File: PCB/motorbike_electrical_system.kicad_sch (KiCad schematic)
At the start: 11 parts, among them U1 L7805, U2 L7805, U3 L7805, U4 ATmega16L-8P

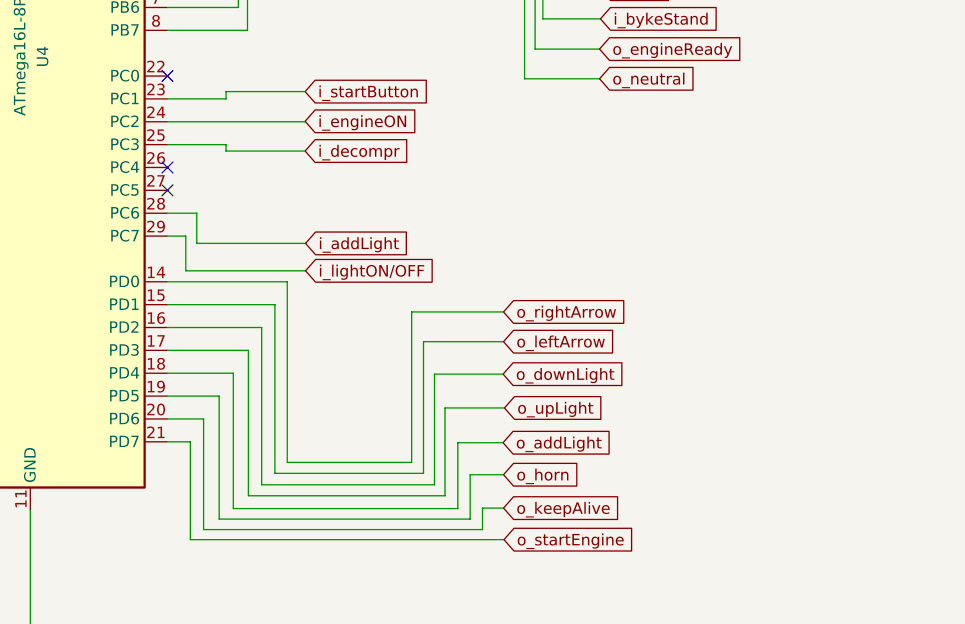
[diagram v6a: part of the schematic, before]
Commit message: RS232 connector added for debug purples
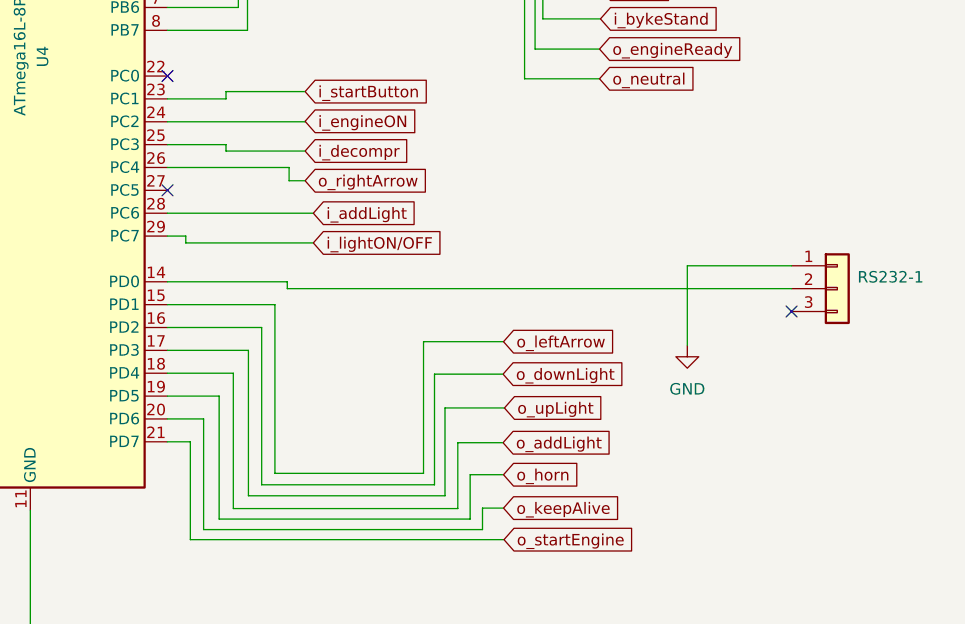
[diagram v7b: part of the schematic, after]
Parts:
- added RS232-1: Conn_01x03, Connector_Hirose:Hirose_DF63M-3P-3.96DSA_1x03_P3.96mm_Vertical, symbol Connector_Generic:Conn_01x03
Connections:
- net GND: now also RS232-1.1 (Pin_1)
- net o_rightArrow: now also U4.26 (PC4); no longer U4.14 (PD0)
- new net: RS232-1.2 (Pin_2), U4.14 (PD0)
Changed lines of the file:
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@@
   )
   (no_connect (at 112.1664 59.182))
-  (no_connect (at 142.6464 109.982))
   (no_connect (at 112.1664 64.262))
   (no_connect (at 142.6464 99.822))
   (no_connect (at 142.6464 66.802))
+  (no_connect (at 211.9884 125.984))
   (no_connect (at 142.6464 112.522))
   (no_connect (at 129.9464 46.482))
@@
     (stroke (width 0) (type default) (color 0 0 0 0))
   )
+  (wire (pts (xy 155.956 123.444) (xy 155.956 122.682))
+    (stroke (width 0) (type default) (color 0 0 0 0))
+  )
   (wire (pts (xy 142.6464 130.302) (xy 151.638 130.302))
     (stroke (width 0) (type default) (color 0 0 0 0))
@@
     (stroke (width 0) (type default) (color 0 0 0 0))
   )
-  (wire (pts (xy 145.8976 115.062) (xy 142.6464 115.062))
+  (wire (pts (xy 142.6464 115.062) (xy 158.8516 115.062))
     (stroke (width 0) (type default) (color 0 0 0 0))
   )
@@
     (stroke (width 0) (type default) (color 0 0 0 0))
   )
-  (wire (pts (xy 145.8976 118.4148) (xy 145.8976 115.062))
-    (stroke (width 0) (type default) (color 0 0 0 0))
-  )
   (wire (pts (xy 80.391 188.087) (xy 103.251 188.087))
     (stroke (width 0) (type default) (color 0 0 0 0))
@@
     (stroke (width 0) (type default) (color 0 0 0 0))
   )
+  (wire (pts (xy 144.6784 118.364) (xy 144.6784 117.602))
+    (stroke (width 0) (type default) (color 0 0 0 0))
+  )
   (wire (pts (xy 61.087 176.53) (xy 60.071 176.53))
     (stroke (width 0) (type default) (color 0 0 0 0))
@@
     (stroke (width 0) (type default) (color 0 0 0 0))
   )
-  (wire (pts (xy 155.956 142.748) (xy 155.956 122.682))
-    (stroke (width 0) (type default) (color 0 0 0 0))
-  )
   (wire (pts (xy 100.076 176.53) (xy 103.251 176.53))
     (stroke (width 0) (type default) (color 0 0 0 0))
@@
     (stroke (width 0) (type default) (color 0 0 0 0))
   )
-  (wire (pts (xy 157.988 118.4148) (xy 145.8976 118.4148))
-    (stroke (width 0) (type default) (color 0 0 0 0))
-  )
   (wire (pts (xy 37.211 169.672) (xy 42.291 169.672))
     (stroke (width 0) (type default) (color 0 0 0 0))
@@
     (stroke (width 0) (type default) (color 0 0 0 0))
   )
+  (wire (pts (xy 142.6464 109.982) (xy 156.1592 109.982))
+    (stroke (width 0) (type default) (color 0 0 0 0))
+  )
   (wire (pts (xy 42.291 169.672) (xy 62.484 169.672))
     (stroke (width 0) (type default) (color 0 0 0 0))
@@
     (stroke (width 0) (type default) (color 0 0 0 0))
   )
+  (wire (pts (xy 156.1592 109.982) (xy 156.1592 111.4552))
+    (stroke (width 0) (type default) (color 0 0 0 0))
+  )
   (wire (pts (xy 157.9372 104.902) (xy 157.9372 104.8512))
     (stroke (width 0) (type default) (color 0 0 0 0))
@@
     (stroke (width 0) (type default) (color 0 0 0 0))
   )
-  (wire (pts (xy 157.988 121.4628) (xy 144.6784 121.4628))
-    (stroke (width 0) (type default) (color 0 0 0 0))
-  )
   (wire (pts (xy 52.451 184.15) (xy 52.451 185.42))
     (stroke (width 0) (type default) (color 0 0 0 0))
   )
-  (wire (pts (xy 179.9844 126.0348) (xy 169.7736 126.0348))
-    (stroke (width 0) (type default) (color 0 0 0 0))
-  )
   (wire (pts (xy 120.777 185.42) (xy 127.4064 185.42))
     (stroke (width 0) (type default) (color 0 0 0 0))
   )
-  (wire (pts (xy 169.7736 126.0348) (xy 169.7736 142.748))
-    (stroke (width 0) (type default) (color 0 0 0 0))
-  )
   (wire (pts (xy 103.251 176.53) (xy 103.251 188.087))
     (stroke (width 0) (type default) (color 0 0 0 0))
@@
     (stroke (width 0) (type default) (color 0 0 0 0))
   )
+  (wire (pts (xy 200.406 120.904) (xy 200.406 129.7432))
+    (stroke (width 0) (type default) (color 0 0 0 0))
+  )
   (wire (pts (xy 108.3564 185.42) (xy 120.777 185.42))
     (stroke (width 0) (type default) (color 0 0 0 0))
@@
     (stroke (width 0) (type default) (color 0 0 0 0))
   )
-  (wire (pts (xy 144.6784 121.4628) (xy 144.6784 117.602))
+  (wire (pts (xy 156.1592 111.4552) (xy 157.9372 111.4552))
     (stroke (width 0) (type default) (color 0 0 0 0))
   )
@@
     (stroke (width 0) (type default) (color 0 0 0 0))
   )
+  (wire (pts (xy 144.6784 118.364) (xy 158.8516 118.364))
+    (stroke (width 0) (type default) (color 0 0 0 0))
+  )
   (wire (pts (xy 151.5364 94.742) (xy 151.5364 84.074))
     (stroke (width 0) (type default) (color 0 0 0 0))
@@
     (stroke (width 0) (type default) (color 0 0 0 0))
   )
-  (wire (pts (xy 169.7736 142.748) (xy 155.956 142.748))
-    (stroke (width 0) (type default) (color 0 0 0 0))
-  )
   (wire (pts (xy 37.211 169.672) (xy 37.211 175.26))
     (stroke (width 0) (type default) (color 0 0 0 0))
@@
     (stroke (width 0) (type default) (color 0 0 0 0))
   )
+  (wire (pts (xy 211.9884 120.904) (xy 200.406 120.904))
+    (stroke (width 0) (type default) (color 0 0 0 0))
+  )
+  (wire (pts (xy 211.9884 123.444) (xy 155.956 123.444))
+    (stroke (width 0) (type default) (color 0 0 0 0))
+  )
   (wire (pts (xy 103.2764 176.53) (xy 108.3564 176.53))
     (stroke (width 0) (type default) (color 0 0 0 0))
@@
     )
   )
-  (global_label "i_addLight" (shape input) (at 157.988 118.4148 0) (fields_autoplaced)
-    (effects (font (size 1.27 1.27)) (justify left))
-    (property "Riferimenti inter-foglio" "${INTERSHEET_REFS}" (id 0) (at 170.0773 118.3354 0)
+  (global_label "i_addLight" (shape input) (at 158.8516 115.062 0) (fields_autoplaced)
+    (effects (font (size 1.27 1.27)) (justify left))
+    (property "Riferimenti inter-foglio" "${INTERSHEET_REFS}" (id 0) (at 170.9409 114.9826 0)
       (effects (font (size 1.27 1.27)) (justify left) hide)
     )
@@
     )
   )
-  (global_label "i_lightON{slash}OFF" (shape input) (at 157.988 121.4628 0) (fields_autoplaced)
-    (effects (font (size 1.27 1.27)) (justify left))
-    (property "Riferimenti inter-foglio" "${INTERSHEET_REFS}" (id 0) (at 173.7663 121.3834 0)
+  (global_label "i_lightON{slash}OFF" (shape input) (at 158.8516 118.364 0) (fields_autoplaced)
+    (effects (font (size 1.27 1.27)) (justify left))
+    (property "Riferimenti inter-foglio" "${INTERSHEET_REFS}" (id 0) (at 174.6299 118.2846 0)
       (effects (font (size 1.27 1.27)) (justify left) hide)
     )
@@
     )
   )
-  (global_label "o_rightArrow" (shape input) (at 179.9844 126.0348 0) (fields_autoplaced)
-    (effects (font (size 1.27 1.27)) (justify left))
-    (property "Riferimenti inter-foglio" "${INTERSHEET_REFS}" (id 0) (at 194.0694 125.9554 0)
+  (global_label "o_rightArrow" (shape input) (at 157.9372 111.4552 0) (fields_autoplaced)
+    (effects (font (size 1.27 1.27)) (justify left))
+    (property "Riferimenti inter-foglio" "${INTERSHEET_REFS}" (id 0) (at 172.0222 111.3758 0)
       (effects (font (size 1.27 1.27)) (justify left) hide)
     )
@@
     (pin "1")
   )
+  (symbol (lib_id "power:GND") (at 200.406 129.7432 0) (unit 1)
+    (in_bom yes) (on_board yes) (fields_autoplaced)
+    (property "Reference" "#PWR0112" (id 0) (at 200.406 136.0932 0)
+      (effects (font (size 1.27 1.27)) hide)
+    )
+    (property "Value" "GND" (id 1) (at 200.406 134.62 0))
+    (property "Footprint" "" (id 2) (at 200.406 129.7432 0)
+      (effects (font (size 1.27 1.27)) hide)
+    )
+    (property "Datasheet" "" (id 3) (at 200.406 129.7432 0)
+      (effects (font (size 1.27 1.27)) hide)
+    )
+    (pin "1")
+  )
+  (symbol (lib_id "Connector_Generic:Conn_01x03") (at 217.0684 123.444 0) (unit 1)
+    (in_bom yes) (on_board yes) (fields_autoplaced)
+    (property "Reference" "RS232-1" (id 0) (at 219.3036 122.1739 0)
+      (effects (font (size 1.27 1.27)) (justify left))
+    )
+    (property "Value" "Conn_01x03" (id 1) (at 219.3036 124.7139 0)
+      (effects (font (size 1.27 1.27)) (justify left) hide)
+    )
+    (property "Footprint" "Connector_Hirose:Hirose_DF63M-3P-3.96DSA_1x03_P3.96mm_Vertical" (id 2) (at 217.0684 123.444 0)
+      (effects (font (size 1.27 1.27)) hide)
+    )
+    (property "Datasheet" "~" (id 3) (at 217.0684 123.444 0)
+      (effects (font (size 1.27 1.27)) hide)
+    )
+    (pin "1")
+    (pin "2")
+    (pin "3")
+  )
   (symbol (lib_id "Device:R_Potentiometer") (at 197.9168 58.0644 0) (mirror y) (unit 1)
     (in_bom yes) (on_board yes)
@@
       (reference "#PWR0111") (unit 1) (value "GND") (footprint "")
     )
+    (path "/84a040ab-9cc4-4162-8dee-269db14b7548"
+      (reference "#PWR0112") (unit 1) (value "GND") (footprint "")
+    )
     (path "/44e17612-9f2f-476d-8e41-268bb036a54a/ca96e50f-3e2b-4429-a303-34aeefffd5a5"
       (reference "Arrow_p1") (unit 1) (value "Conn_01x03") (footprint "Connector_Wire:SolderWire-1.5sqmm_1x03_P6mm_D1.7mm_OD3mm")
@@
       (reference "RA49") (unit 1) (value "100K") (footprint "Resistor_THT:R_Axial_DIN0207_L6.3mm_D2.5mm_P7.62mm_Horizontal")
     )
+    (path "/9642f9cf-4b46-422a-a864-ecd9c3909353"
+      (reference "RS232-1") (unit 1) (value "Conn_01x03") (footprint "Connector_Hirose:Hirose_DF63M-3P-3.96DSA_1x03_P3.96mm_Vertical")
+    )
     (path "/dfeffa1f-9119-4780-8aed-ab76c9242c17"
